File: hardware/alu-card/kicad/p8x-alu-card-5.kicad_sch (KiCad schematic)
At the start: 1 part, among them J1 MABC96R

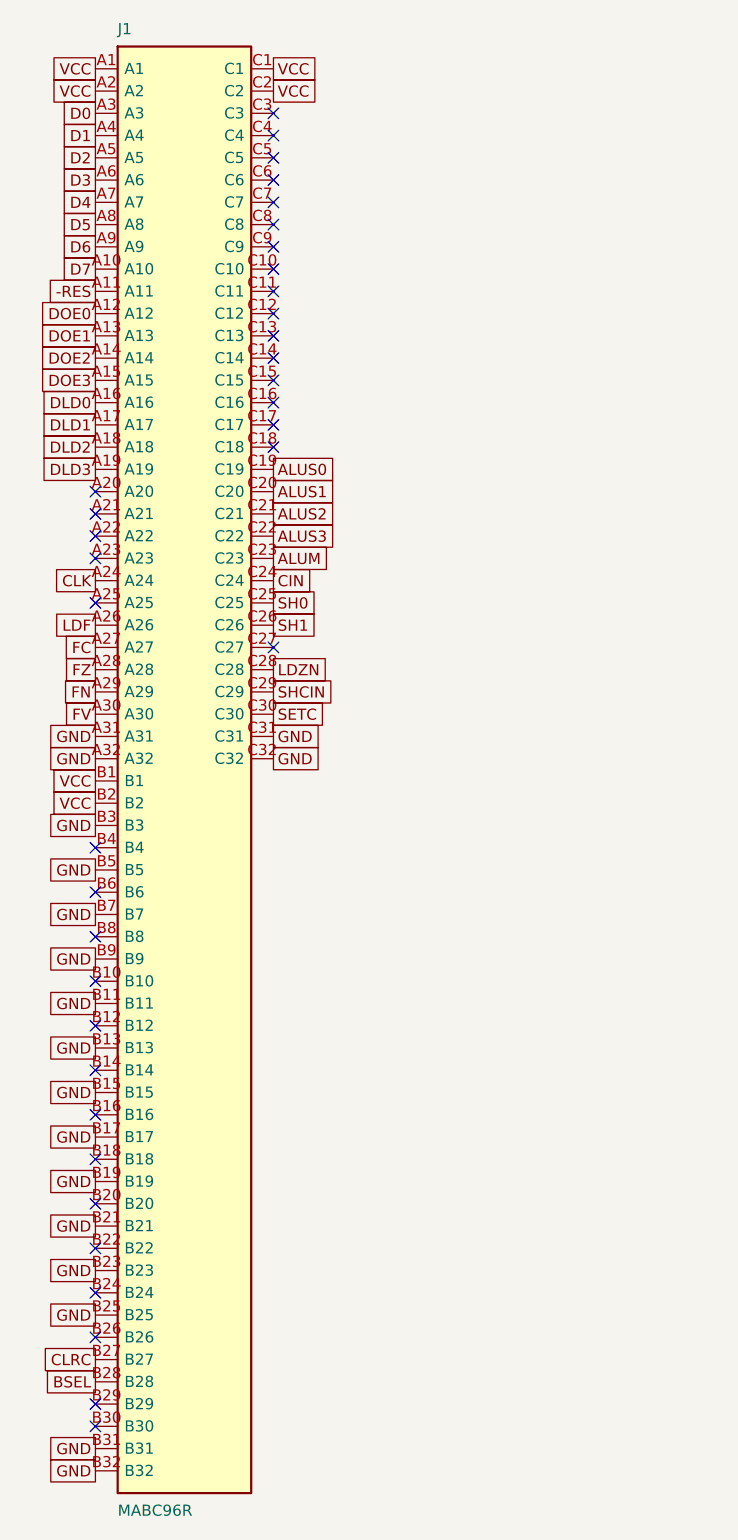
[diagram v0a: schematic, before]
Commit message: feat(sch): draw every P8X card schematic by function
Extend the functional-sheet grouping from the io-card to the control,
regbank, alu, memory, cf, ps2 and bustest cards. functional_sheets now
attaches unnamed glue gates, LEDs, resistors and connectors to the block
they share the most local nets with, so each block lists only its main
parts. A net with two or more pins on a sheet is now wired there even if
it continues elsewhere (its global name label rides on the wire), and
every wire is oriented by drawing side. The regbank gets one pointer per
sheet; the ps2 latches share a sheet with the AVR so the mailbox bus is
drawn. The bustest probe resistors use a straight-order RNISO8DSTR
drawing (the reversed B side forced every wire to cross and the sheet
fell back to labels). build_sch.sh now shows ELK fallbacks and clears old
numbered sheets before a build. All eight netlists match the boards,
ERC 0 errors; the boards change only in footprint link paths.

Co-Authored-By: Claude Opus 5.5 <noreply@anthropic.com>
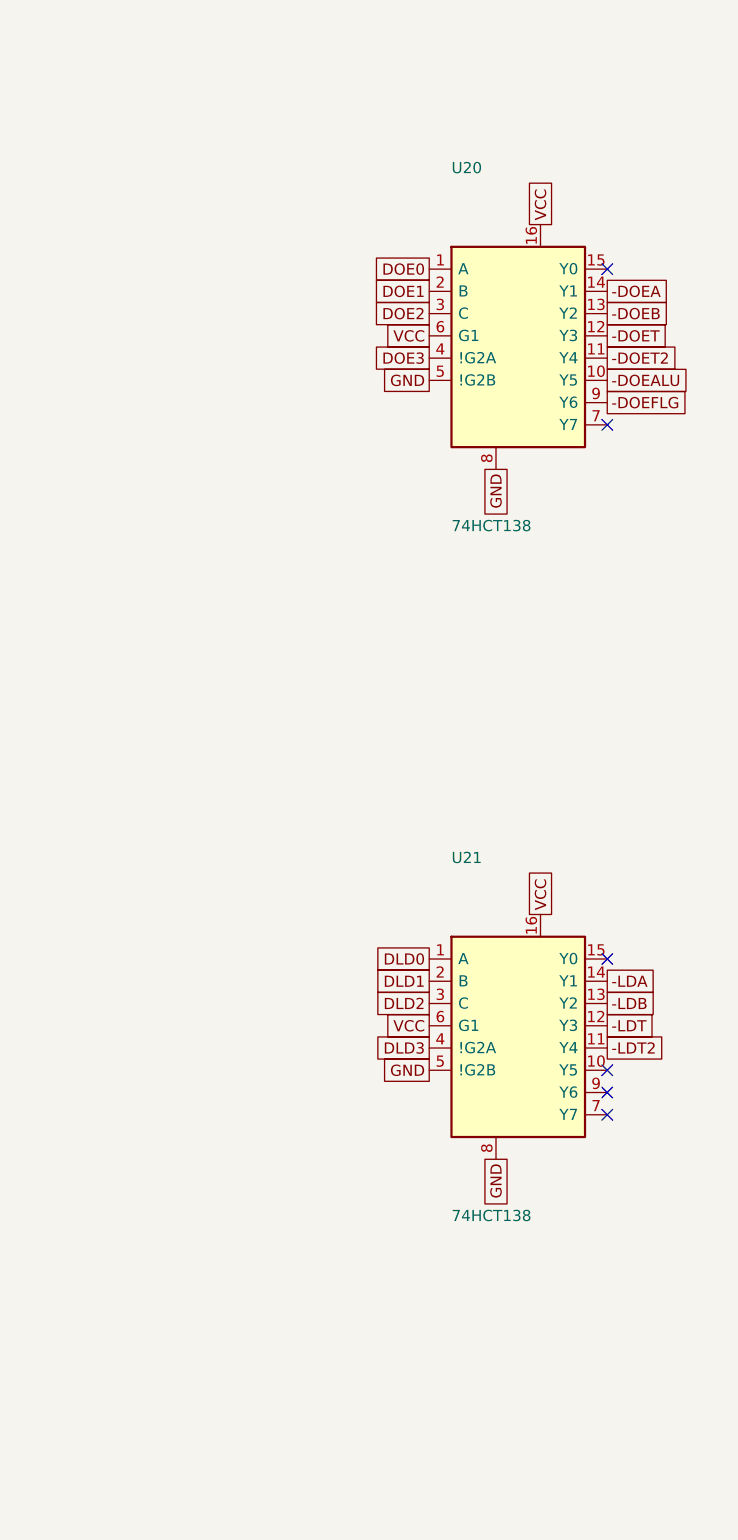
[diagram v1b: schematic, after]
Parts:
- removed J1: MABC96R, Connector_DIN:DIN41612_C_3x32_Male_Horizontal_THT, symbol p8x:DIN96C
- added U20, U21: 74HCT138, Package_DIP:DIP-16_W7.62mm, symbol p8x:74138
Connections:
- net DLD0: now also U21.1 (A)
- net DLD1: now also U21.2 (B)
- net DLD2: now also U21.3 (C)
- net DLD3: now also U21.4 (!G2A)
- net DOE0: now also U20.1 (A)
- net DOE1: now also U20.2 (B)
- net DOE2: now also U20.3 (C)
- net DOE3: now also U20.4 (!G2A)
- net GND: now also U20.5 (!G2B), U20.8, U21.5 (!G2B), U21.8
- net VCC: now also U20.16, U20.6 (G1), U21.16, U21.6 (G1)
- new net -DOEA: U20.14 (Y1)
- new net -DOEALU: U20.10 (Y5)
- new net -DOEB: U20.13 (Y2)
- new net -DOEFLG: U20.9 (Y6)
- new net -DOET: U20.12 (Y3)
- new net -DOET2: U20.11 (Y4)
- new net -LDA: U21.14 (Y1)
- new net -LDB: U21.13 (Y2)
- new net -LDT: U21.12 (Y3)
- new net -LDT2: U21.11 (Y4)
- no-connect marks 36 -> 6
